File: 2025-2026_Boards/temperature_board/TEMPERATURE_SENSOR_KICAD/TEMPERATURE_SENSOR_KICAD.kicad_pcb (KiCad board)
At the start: 2 copper layers, 73.3 x 75.8 mm, 88 parts, among them J1 LCD Connector Pinout, J10 Conn_01x02_Pin, J11 Conn_01x02_Pin, J12 Conn_01x02_Pin, J13 Conn_01x02_Pin, J14 Conn_01x02_Pin, J15 Conn_01x02_Pin, J16 Conn_01x02_Pin, J17 Conn_01x02_Pin, J18 Conn_01x02_Pin, J19 Conn_01x02_Pin, J2 Conn_01x02_Pin, J20 Conn_01x02_Pin, J21 Conn_01x02_Pin, J22 Conn_01x02_Pin, J23 Conn_01x02_Pin, J24 Conn_01x03_Socket, J25 Conn_01x03_Socket, J3 Conn_01x02_Pin, J4 Conn_01x02_Pin, J5 Conn_01x02_Pin, J6 Conn_01x02_Pin, J7 Conn_01x02_Pin, J8 Conn_01x02_Pin, J9 Conn_01x02_Pin, Q1 Q_NPN_BCE, Q3 Q_NPN_BCE, Q4 Q_NPN_BCE, Q5 Q_PNP_BCE, U1 STM32G431CBT6, U2 TMP235A4DBZR, U3 AMS1117-3.3, U4 TCAN1057AEV-Q1, U5 TPS62932DRLR

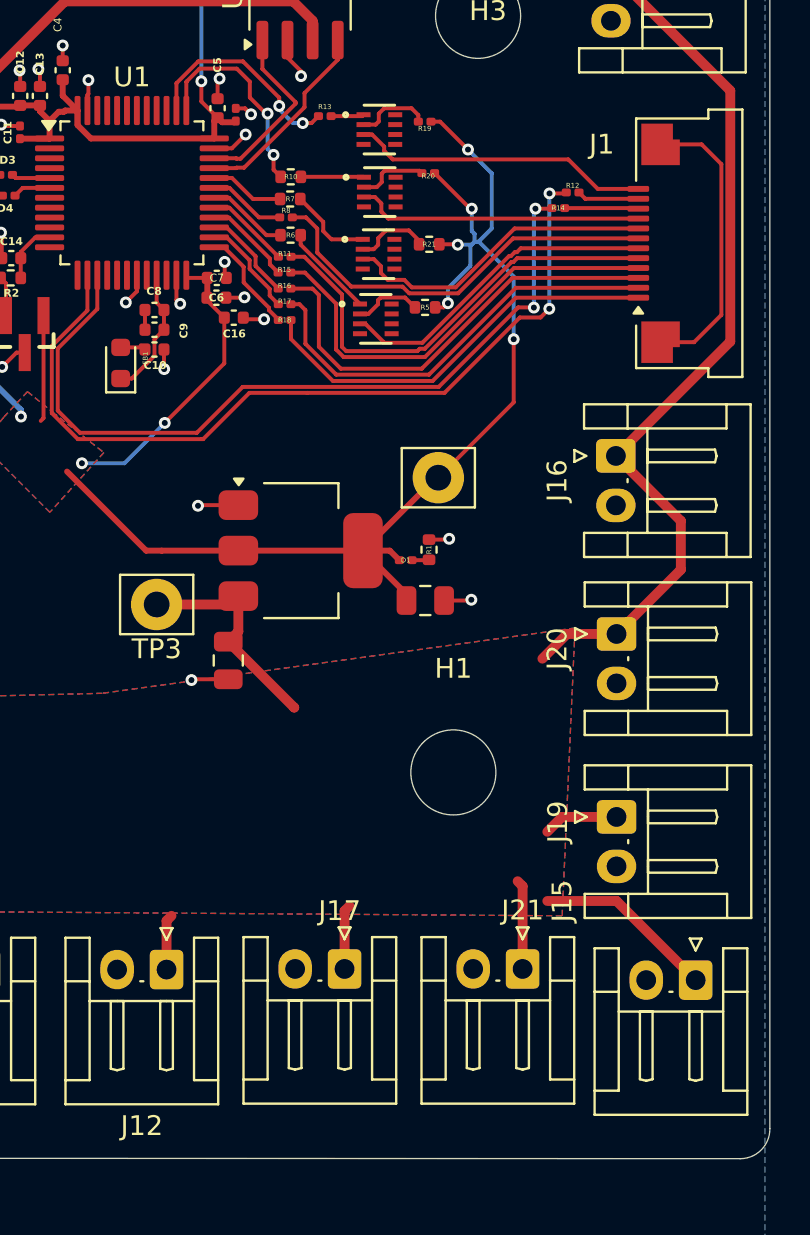
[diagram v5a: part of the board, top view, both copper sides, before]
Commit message: moved 5v regulator closer
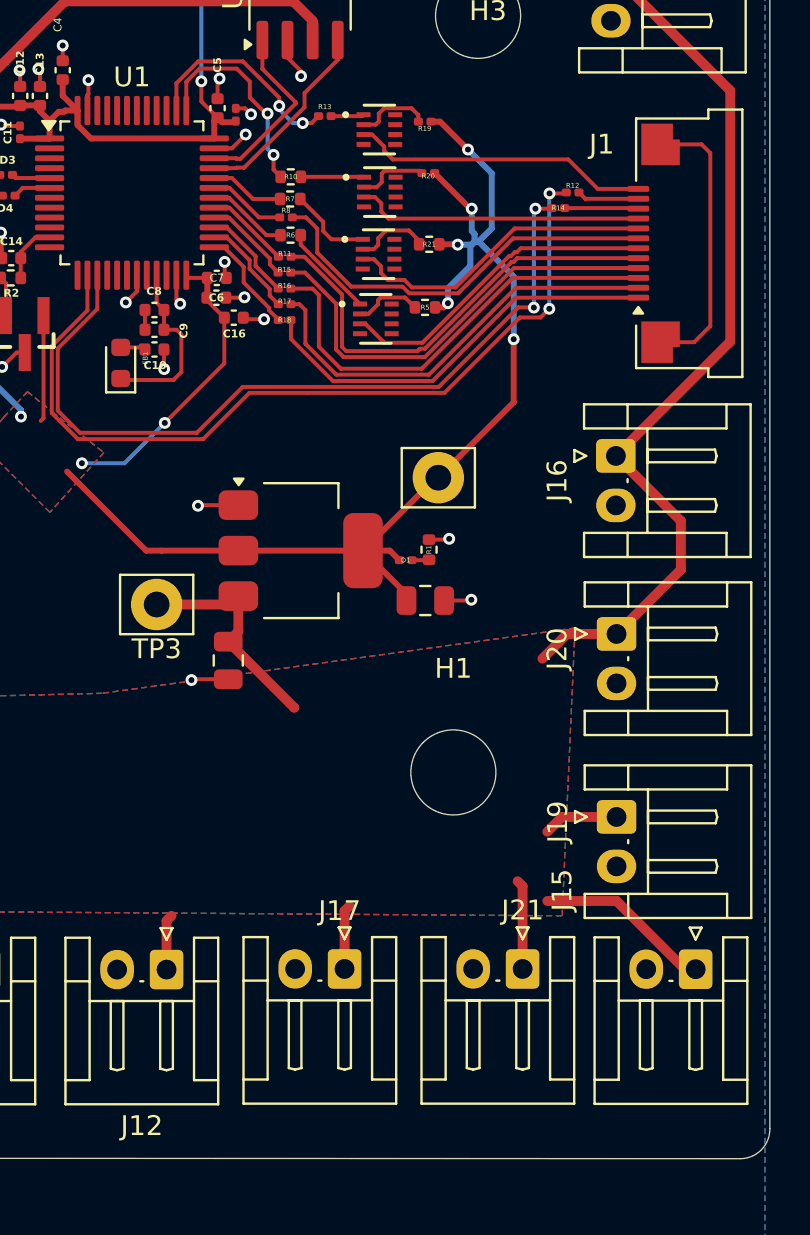
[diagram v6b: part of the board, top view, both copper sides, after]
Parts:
- moved J15 0.55 mm to (141.2, 163.2)
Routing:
- net +3.3VA: track 6.61 -> 9.06 mm
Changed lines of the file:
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@@
 	(footprint "Connector_JST:JST_EH_S2B-EH_1x02_P2.50mm_Horizontal"
 		(layer "F.Cu")
-		(at 141.25 163.75 180)
+		(at 141.25 163.1975 180)
 		(descr "JST EH series connector, S2B-EH (http://www.jst-mfg.com/product/pdf/eng/eEH.pdf), generated with kicad-footprint-generator")
 		(tags "connector JST EH horizontal")
@@
 			)
 			(layer "F.CrtYd")
+			(net 102865361)
 		)
 		(fp_line
@@
 			)
 			(layer "F.CrtYd")
+			(net 102865361)
 		)
 		(fp_line
@@
 			)
 			(layer "F.CrtYd")
+			(net 102865361)
 		)
 		(fp_line
@@
 			)
 			(layer "F.CrtYd")
+			(net 102865361)
 		)
 		(fp_line
@@
 			)
 			(layer "F.Fab")
+			(net 102865361)
 		)
 		(fp_line
@@
 			)
 			(layer "F.Fab")
+			(net 102865361)
 		)
 		(fp_line
@@
 			)
 			(layer "F.Fab")
+			(net 102865361)
 		)
 		(fp_line
@@
 			)
 			(layer "F.Fab")
+			(net 102865361)
 		)
 		(fp_text user "${REFERENCE}"
@@
 			)
 			(layer "F.SilkS")
+			(net 102865361)
 		)
 		(fp_line
@@
 			)
 			(layer "F.SilkS")
+			(net 102865361)
 		)
 		(fp_line
@@
 			)
 			(layer "F.CrtYd")
+			(net 102865361)
 		)
 		(fp_line
@@
 			)
 			(layer "F.CrtYd")
+			(net 102865361)
 		)
 		(fp_line
@@
 			)
 			(layer "F.CrtYd")
+			(net 102865361)
 		)
 		(fp_line
@@
 			)
 			(layer "F.CrtYd")
+			(net 102865361)
 		)
 		(fp_line
@@
 			)
 			(layer "F.Fab")
+			(net 102865361)
 		)
 		(fp_line
@@
 			)
 			(layer "F.Fab")
+			(net 102865361)
 		)
 		(fp_line
@@
 			)
 			(layer "F.Fab")
+			(net 102865361)
 		)
 		(fp_line
@@
 			)
 			(layer "F.Fab")
+			(net 102865361)
 		)
 		(fp_text user "${REFERENCE}"
@@
 		(start 132.05 134.54)
 		(end 132.05 131.35)
-		(width 0.2)
+		(width 0.3)
 		(layer "F.Cu")
 		(net 2)
@@
 		(start 129.2 126.55)
 		(end 129.22 126.57)
-		(width 0.2)
+		(width 0.3)
 		(layer "F.Cu")
 		(net 2)
@@
 		(start 129.85 124.75)
 		(end 129.93 124.75)
-		(width 0.2)
+		(width 0.3)
 		(layer "F.Cu")
 		(net 2)
@@
 		(start 128.515859 129.74)
 		(end 128.72586 129.529999)
-		(width 0.2)
+		(width 0.3)
 		(layer "F.Cu")
 		(net 2)
@@
 		(start 127.87 120.35)
 		(end 128.33 120.35)
-		(width 0.2)
+		(width 0.3)
 		(layer "F.Cu")
 		(net 2)
@@
 		(start 128.33 120.35)
 		(end 129.74 121.76)
-		(width 0.2)
+		(width 0.3)
 		(layer "F.Cu")
 		(net 2)
@@
 		(start 128.08 129.74)
 		(end 128.515859 129.74)
-		(width 0.2)
+		(width 0.3)
 		(layer "F.Cu")
 		(net 2)
@@
 		(start 128.05 122.95)
 		(end 129.85 124.75)
-		(width 0.2)
+		(width 0.3)
 		(layer "F.Cu")
 		(net 2)
@@
 		(start 128.24 138.35)
 		(end 132.05 134.54)
-		(width 0.2)
+		(width 0.3)
 		(layer "F.Cu")
 		(net 2)
@@
 		(start 128.29 126.55)
 		(end 129.2 126.55)
-		(width 0.2)
+		(width 0.3)
 		(layer "F.Cu")
 		(net 2)
@@
 		(start 129.858607 126.641393)
 		(end 130.07 126.43)
-		(width 0.2)
+		(width 0.3)
 		(layer "B.Cu")
 		(net 2)
@@
 		(start 129.858607 127.641393)
 		(end 128.72586 128.77414)
-		(width 0.2)
+		(width 0.3)
 		(layer "B.Cu")
 		(net 2)
@@
 		(start 129.93 126.57)
 		(end 130.07 126.43)
-		(width 0.2)
+		(width 0.3)
 		(layer "B.Cu")
 		(net 2)
@@
 		(start 129.74 121.76)
 		(end 130.94 122.96)
-		(width 0.2)
+		(width 0.3)
 		(layer "B.Cu")
 		(net 2)
@@
 		(start 130.3 126.43)
 		(end 132.05 128.18)
-		(width 0.2)
+		(width 0.3)
 		(layer "B.Cu")
 		(net 2)
@@
 		(start 130.07 126.43)
 		(end 130.2 126.43)
-		(width 0.2)
+		(width 0.3)
 		(layer "B.Cu")
 		(net 2)
@@
 		(start 130.07 126.43)
 		(end 130.07 126.02)
-		(width 0.2)
+		(width 0.3)
 		(layer "B.Cu")
 		(net 2)
@@
 		(start 130.94 125.75)
 		(end 130.26 126.43)
-		(width 0.2)
+		(width 0.3)
 		(layer "B.Cu")
 		(net 2)
@@
 		(start 128.72586 128.77414)
 		(end 128.72586 129.529999)
-		(width 0.2)
+		(width 0.3)
 		(layer "B.Cu")
 		(net 2)
@@
 		(start 130.26 126.43)
 		(end 130.2 126.43)
-		(width 0.2)
+		(width 0.3)
 		(layer "B.Cu")
 		(net 2)
@@
 		(start 129.93 125.88)
 		(end 130.07 126.02)
-		(width 0.2)
+		(width 0.3)
 		(layer "B.Cu")
 		(net 2)
@@
 		(start 130.2 126.43)
 		(end 130.3 126.43)
-		(width 0.2)
+		(width 0.3)
 		(layer "B.Cu")
 		(net 2)
@@
 		(start 130.94 122.96)
 		(end 130.94 125.75)
-		(width 0.2)
+		(width 0.3)
 		(layer "B.Cu")
 		(net 2)
@@
 		(start 129.22 126.57)
 		(end 129.93 126.57)
-		(width 0.2)
+		(width 0.3)
 		(layer "B.Cu")
 		(net 2)
@@
 		(start 129.858607 127.641393)
 		(end 129.858607 126.641393)
-		(width 0.2)
+		(width 0.3)
 		(layer "B.Cu")
 		(net 2)
@@
 		(start 132.05 128.18)
 		(end 132.05 131.35)
-		(width 0.2)
+		(width 0.3)
 		(layer "B.Cu")
 		(net 2)
@@
 		(start 129.93 124.75)
 		(end 129.93 125.88)
-		(width 0.2)
+		(width 0.3)
 		(layer "B.Cu")
 		(net 2)
@@
 	)
 	(segment
-		(start 113.89 131.35)
-		(end 113.89 132.186128)
+		(start 115.25 133.01)
+		(end 114.85 133.41)
 		(width 0.2)
 		(layer "F.Cu")
@@
 	)
 	(segment
-		(start 113.89 132.186128)
-		(end 112.738628 133.3375)
+		(start 114.37 130.87)
+		(end 115.01 130.87)
 		(width 0.2)
 		(layer "F.Cu")
@@
 	)
 	(segment
+		(start 115.25 131.11)
+		(end 115.25 133.01)
+		(width 0.2)
+		(layer "F.Cu")
+		(net 4)
+	)
+	(segment
 		(start 114 129.5)
 		(end 114.37 129.87)
@@
 	)
 	(segment
-		(start 114.37 130.87)
-		(end 113.89 131.35)
+		(start 112.2525 133.41)
+		(end 112.18 133.3375)
 		(width 0.2)
 		(layer "F.Cu")
@@
 	)
 	(segment
-		(start 112.738628 133.3375)
-		(end 112.18 133.3375)
+		(start 114.85 133.41)
+		(end 112.2525 133.41)
+		(width 0.2)
+		(layer "F.Cu")
+		(net 4)
+	)
+	(segment
+		(start 115.01 130.87)
+		(end 115.25 131.11)
 		(width 0.2)
 		(layer "F.Cu")
@@
 	)
 	(segment
-		(start 139.475 131.5)
-		(end 141.17 131.5)
+		(start 141.55 121.5)
+		(end 139.475 121.5)
 		(width 0.2)
 		(layer "F.Cu")
@@
 	)
 	(segment
-		(start 142.55 122.5)
-		(end 141.55 121.5)
+		(start 141.17 131.5)
+		(end 141.99 130.68)
 		(width 0.2)
 		(layer "F.Cu")
@@
 	)
 	(segment
-		(start 142.55 130.12)
-		(end 142.55 122.5)
+		(start 141.99 121.94)
+		(end 141.55 121.5)
 		(width 0.2)
 		(layer "F.Cu")
@@
 	)
 	(segment
-		(start 141.17 131.5)
-		(end 142.55 130.12)
+		(start 139.475 131.5)
+		(end 141.17 131.5)
 		(width 0.2)
 		(layer "F.Cu")
@@
 	)
 	(segment
-		(start 141.55 121.5)
-		(end 139.475 121.5)
+		(start 141.99 130.68)
+		(end 141.99 121.94)
 		(width 0.2)
 		(layer "F.Cu")

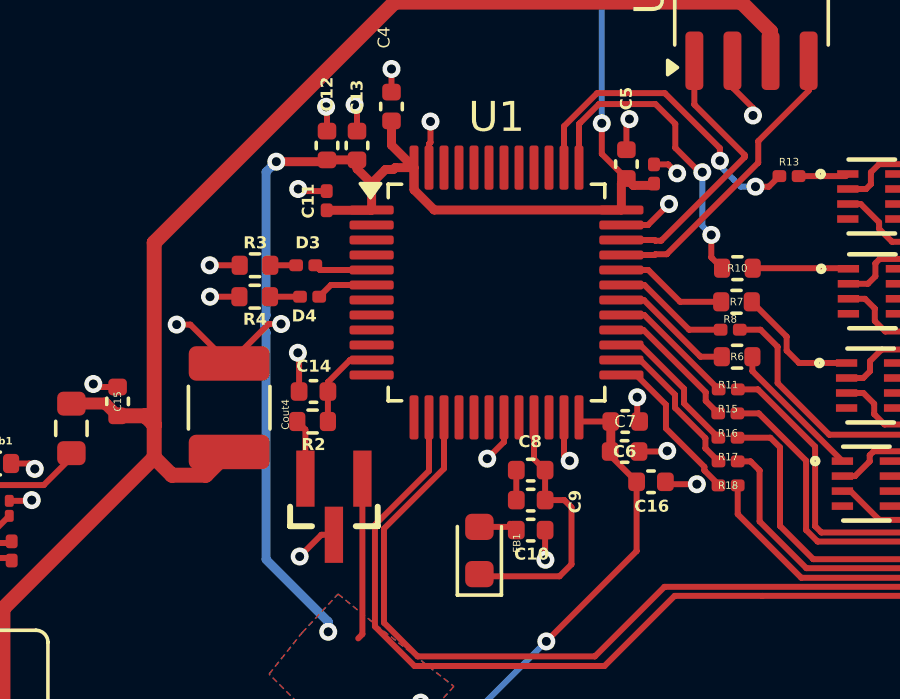
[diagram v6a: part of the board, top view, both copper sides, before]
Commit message: moved 3.3v decoup cap somewhere else
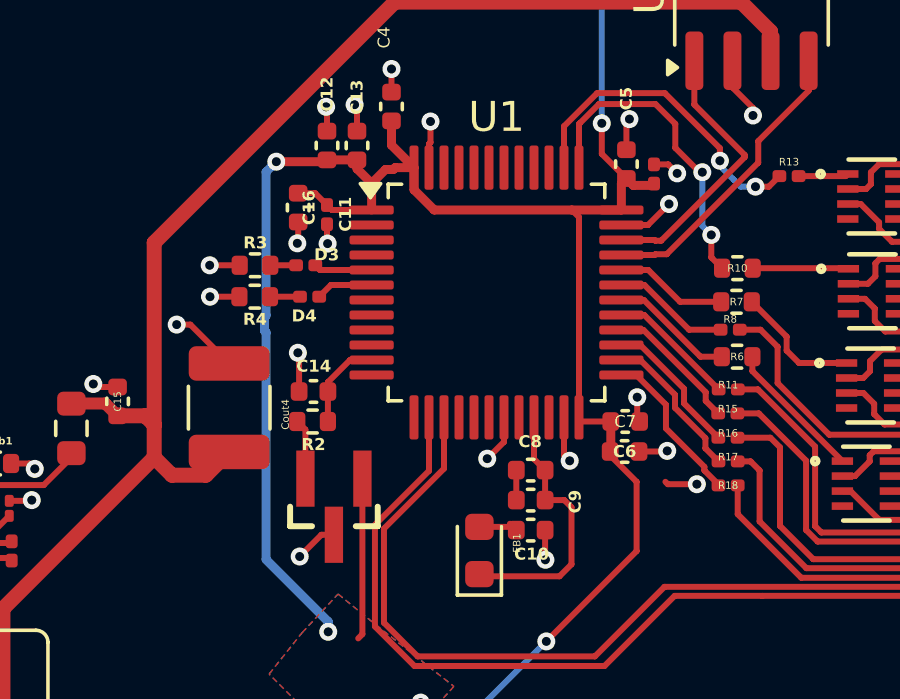
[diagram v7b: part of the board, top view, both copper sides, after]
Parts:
- moved C16 14.9 mm to (106.1, 121.1), turned to -90 degrees
- moved C11 0.47 mm to (107.1, 121.4), turned to -90 degrees
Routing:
- net +3.3V: track 135.2 -> 143.3 mm
- net GND: track 49.0 -> 47.1 mm

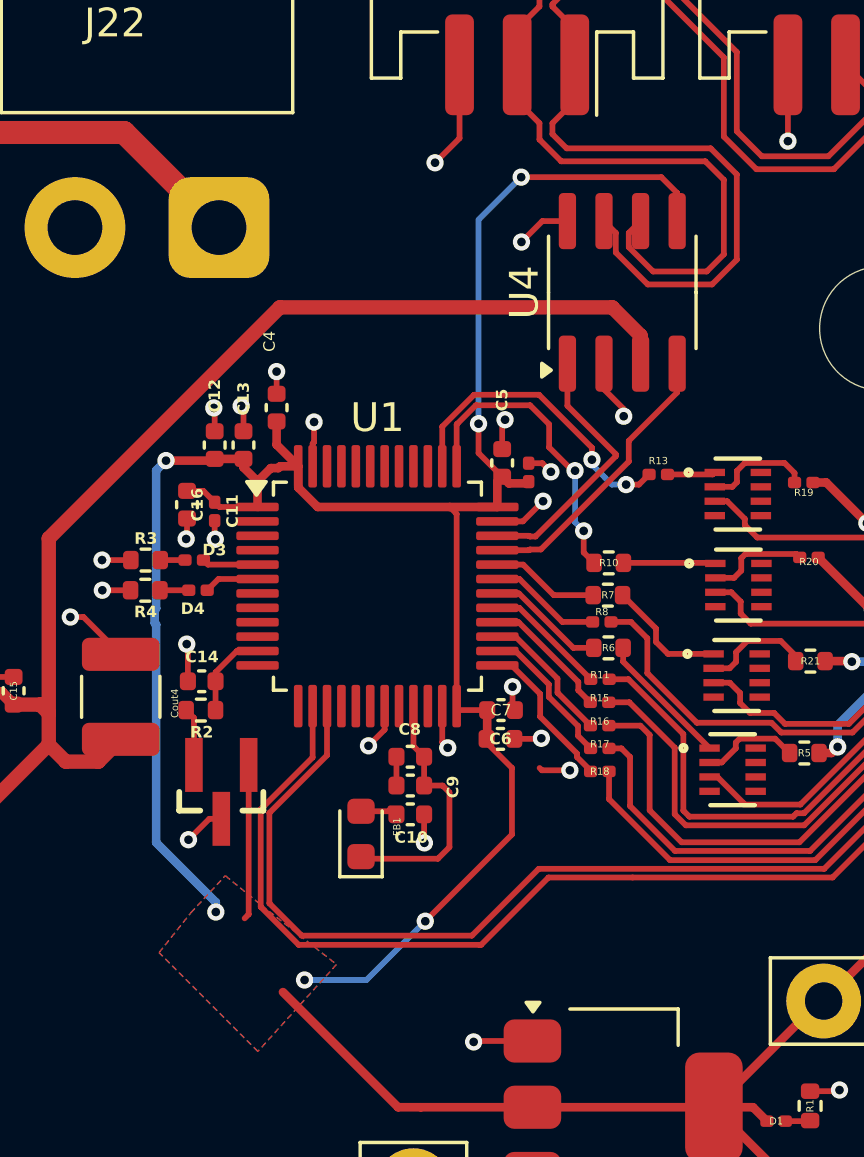
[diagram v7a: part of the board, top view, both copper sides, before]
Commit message: moved 3.3v decoup cap somewhere else
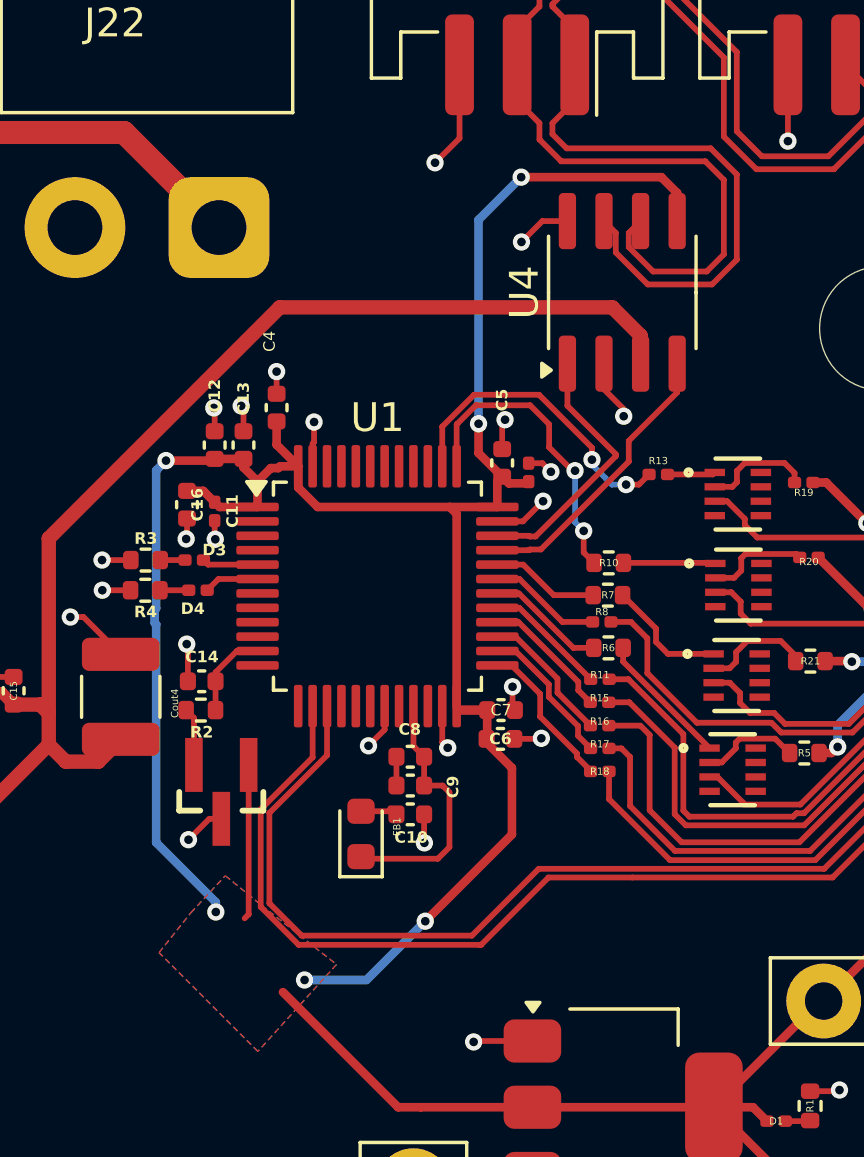
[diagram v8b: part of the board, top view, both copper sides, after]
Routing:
- net GND: track 47.1 -> 46.0 mm, vias 34 -> 33
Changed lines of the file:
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@@
 			)
 			(layer "F.CrtYd")
-			(net 418580696)
+			(net 1)
 		)
 		(fp_line
@@
 			)
 			(layer "F.CrtYd")
-			(net 418580696)
+			(net 1)
 		)
 		(fp_line
@@
 			)
 			(layer "F.CrtYd")
-			(net 418580696)
+			(net 1)
 		)
 		(fp_line
@@
 			)
 			(layer "F.CrtYd")
-			(net 418580696)
+			(net 1)
 		)
 		(fp_line
@@
 			)
 			(layer "F.Fab")
-			(net 418580696)
+			(net 1)
 		)
 		(fp_line
@@
 			)
 			(layer "F.Fab")
-			(net 418580696)
+			(net 1)
 		)
 		(fp_line
@@
 			)
 			(layer "F.Fab")
-			(net 418580696)
+			(net 1)
 		)
 		(fp_line
@@
 			)
 			(layer "F.Fab")
-			(net 418580696)
+			(net 1)
 		)
 		(fp_text user "${REFERENCE}"
@@
 			)
 			(layer "F.SilkS")
-			(net 418580696)
+			(net 1)
 		)
 		(fp_line
@@
 			)
 			(layer "F.SilkS")
-			(net 418580696)
+			(net 1)
 		)
 		(fp_line
@@
 			)
 			(layer "F.CrtYd")
-			(net 418580696)
+			(net 1)
 		)
 		(fp_line
@@
 			)
 			(layer "F.CrtYd")
-			(net 418580696)
+			(net 1)
 		)
 		(fp_line
@@
 			)
 			(layer "F.CrtYd")
-			(net 418580696)
+			(net 1)
 		)
 		(fp_line
@@
 			)
 			(layer "F.CrtYd")
-			(net 418580696)
+			(net 1)
 		)
 		(fp_line
@@
 			)
 			(layer "F.Fab")
-			(net 418580696)
+			(net 1)
 		)
 		(fp_line
@@
 			)
 			(layer "F.Fab")
-			(net 418580696)
+			(net 1)
 		)
 		(fp_line
@@
 			)
 			(layer "F.Fab")
-			(net 418580696)
+			(net 1)
 		)
 		(fp_line
@@
 			)
 			(layer "F.Fab")
-			(net 418580696)
+			(net 1)
 		)
 		(fp_text user "${REFERENCE}"
@@
 	)
 	(segment
-		(start 118.46 130.34)
-		(end 118.38 130.26)
-		(width 0.2)
-		(layer "F.Cu")
-		(net 1)
-	)
-	(segment
 		(start 90.33 134.67)
 		(end 90.33 133.85)
@@
 	)
 	(segment
-		(start 119.43 130.34)
-		(end 118.46 130.34)
-		(width 0.2)
-		(layer "F.Cu")
-		(net 1)
-	)
-	(segment
 		(start 127.77 141.48)
 		(end 128.75 141.48)
@@
 	)
 	(via
-		(at 119.43 130.34)
-		(size 0.6)
-		(drill 0.3)
-		(layers "F.Cu" "B.Cu")
-		(net 1)
-	)
-	(via
 		(at 108.02 117.69)
 		(size 0.6)
@@
 		(start 115.5 121.44)
 		(end 115.5 128.1125)
-		(width 0.2)
+		(width 0.3)
 		(layer "F.Cu")
 		(net 2)
@@
 		(start 117.42 130.26)
 		(end 117.42 132.57)
-		(width 0.2)
+		(width 0.3)
 		(layer "F.Cu")
 		(net 2)
@@
 		(start 123.155 110.300001)
 		(end 122.604999 109.75)
-		(width 0.2)
+		(width 0.3)
 		(layer "F.Cu")
 		(net 2)
@@
 		(start 122.604999 109.75)
 		(end 117.74 109.75)
-		(width 0.2)
+		(width 0.3)
 		(layer "F.Cu")
 		(net 2)
@@
 		(start 116.26 119.33)
 		(end 117.08 120.15)
-		(width 0.2)
+		(width 0.3)
 		(layer "F.Cu")
 		(net 2)
@@
 		(start 107.265 121.2)
 		(end 107.1 121.035)
-		(width 0.2)
+		(width 0.3)
 		(layer "F.Cu")
 		(net 2)
@@
 		(start 116.26 118.31)
 		(end 116.26 119.33)
-		(width 0.2)
+		(width 0.3)
 		(layer "F.Cu")
 		(net 2)
@@
 		(start 123.155 111.275)
 		(end 123.155 110.300001)
-		(width 0.2)
+		(width 0.3)
 		(layer "F.Cu")
 		(net 2)
@@
 		(start 115.26 121.2)
 		(end 115.5 121.44)
-		(width 0.2)
+		(width 0.3)
 		(layer "F.Cu")
 		(net 2)
@@
 		(start 106.14 120.64)
 		(end 106.705 120.64)
-		(width 0.2)
+		(width 0.3)
 		(layer "F.Cu")
 		(net 2)
@@
 		(start 106.705 120.64)
 		(end 107.1 121.035)
-		(width 0.2)
+		(width 0.3)
 		(layer "F.Cu")
 		(net 2)
@@
 		(start 116.54 129.38)
 		(end 117.42 130.26)
-		(width 0.2)
+		(width 0.3)
 		(layer "F.Cu")
 		(net 2)
@@
 		(start 116.54 129.25)
 		(end 116.54 129.38)
-		(width 0.2)
+		(width 0.3)
 		(layer "F.Cu")
 		(net 2)
@@
 		(start 117.42 132.57)
 		(end 114.41 135.58)
-		(width 0.2)
+		(width 0.3)
 		(layer "F.Cu")
 		(net 2)
@@
 		(start 116.56 128.25)
 		(end 115.573979 128.25)
-		(width 0.2)
+		(width 0.33)
 		(layer "F.Cu")
 		(net 2)
@@
 		(start 108.5875 121.2)
 		(end 107.265 121.2)
-		(width 0.2)
+		(width 0.3)
 		(layer "F.Cu")
 		(net 2)
@@
 		(start 117.74 109.75)
 		(end 116.26 111.23)
-		(width 0.2)
+		(width 0.3)
 		(layer "B.Cu")
 		(net 2)
@@
 		(start 114.41 135.58)
 		(end 112.37 137.62)
-		(width 0.2)
+		(width 0.3)
 		(layer "B.Cu")
 		(net 2)
@@
 		(start 116.26 111.23)
 		(end 116.26 118.31)
-		(width 0.2)
+		(width 0.3)
 		(layer "B.Cu")
 		(net 2)
@@
 		(start 112.37 137.62)
 		(end 110.22 137.62)
-		(width 0.2)
+		(width 0.3)
 		(layer "B.Cu")
 		(net 2)
